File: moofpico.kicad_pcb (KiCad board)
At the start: 2 copper layers, 85.7 x 62.9 mm, 21 parts, among them J1 Conn_01x04, J100 Bus_Apple_II_Card_Side, J2 Micro_SD_Card_Det2, Q1 BS170, SW1 SW_DIP_x02, U2 74F11, U3 74LVC245, U4 74LVC245, U5 74LVC245, U6 RaspberryPi_Pico

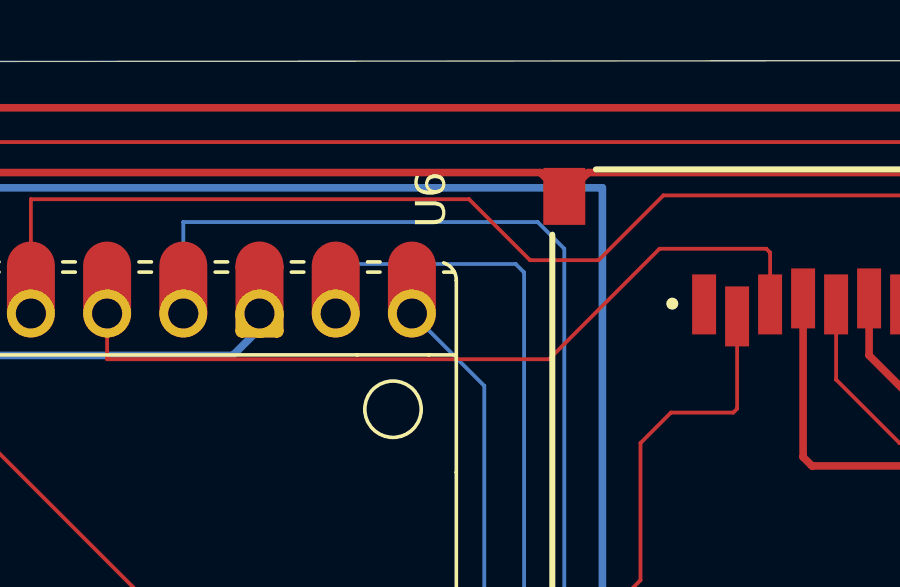
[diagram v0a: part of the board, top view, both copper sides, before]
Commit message: I do love how resynchronizing with the schematic changes all the UUIDs
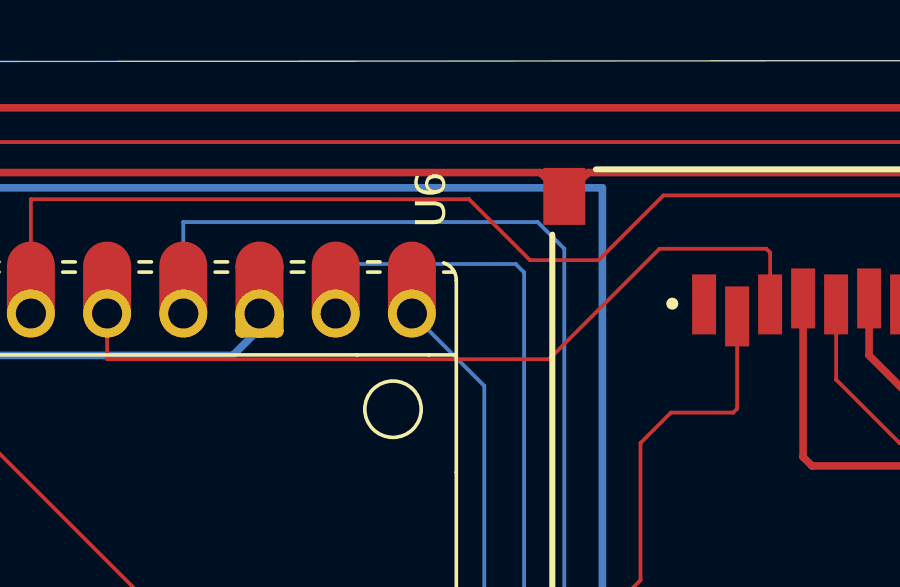
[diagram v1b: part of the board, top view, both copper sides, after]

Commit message: this side towards enemy
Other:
- board text added: "<- KBD"
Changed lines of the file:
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@@
 		(fp_arc
 			(start 10.579676 25.189937)
-			(mid 10.357946 25.493957)
+			(mid 10.357958 25.493991)
 			(end 10 25.61)
 			(stroke
@@
 		(layer "Edge.Cuts")
 	)
+	(gr_text "<- KBD"
+		(at 103.632 87.757 0)
+		(layer "F.SilkS")
+		(effects
+			(font
+				(size 0.8128 0.8128)
+				(thickness 0.1524)
+				(bold yes)
+			)
+			(justify left bottom)
+		)
+	)
 	(segment

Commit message: more faffing about with moving components
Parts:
- moved C5 1.15 mm to (172.0, 124.0)
- moved R4 0.66 mm to (174.5, 117.5)
- moved C3 0.31 mm to (171.0, 112.3)
- moved C1 0.26 mm to (174.0, 100.0)
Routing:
- net GND: track 366.8 -> 375.3 mm
- net +5V: track 48.2 -> 48.8 mm

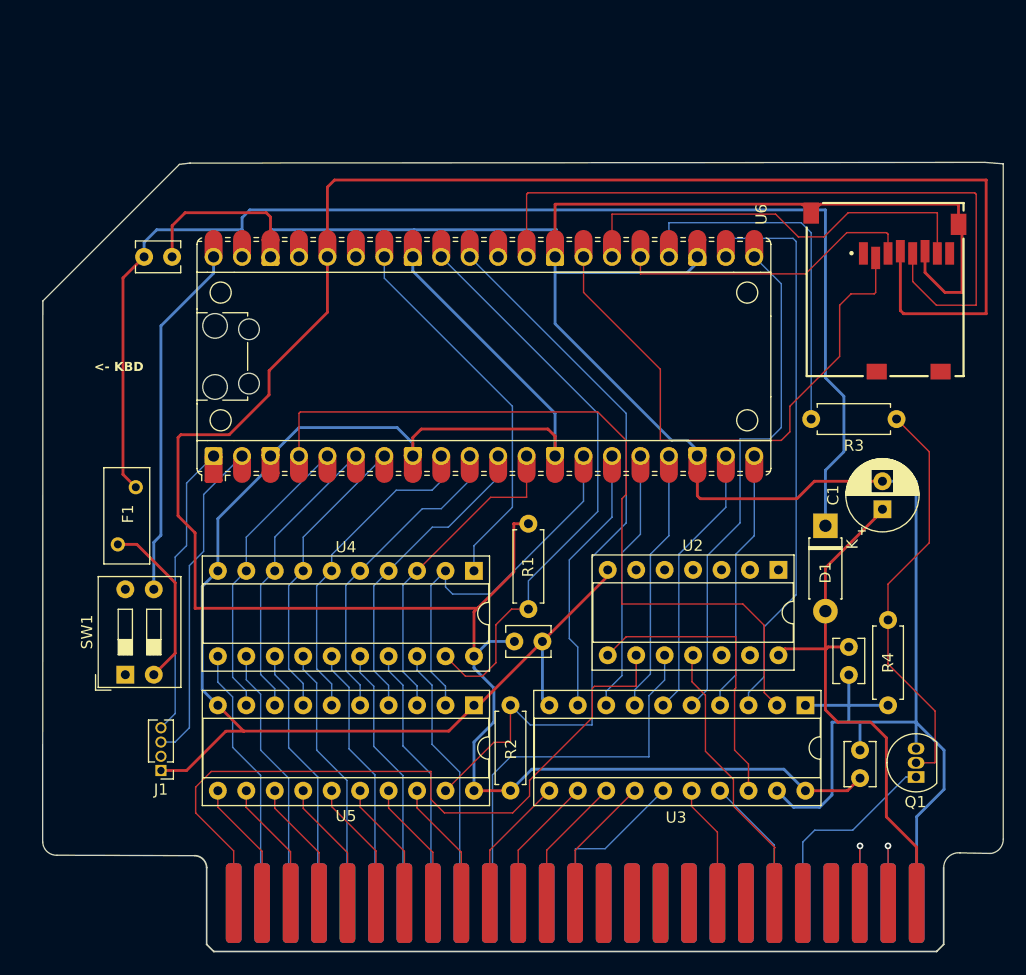
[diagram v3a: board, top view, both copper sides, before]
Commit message: checkpoint: kicad 8.0.1, move components around
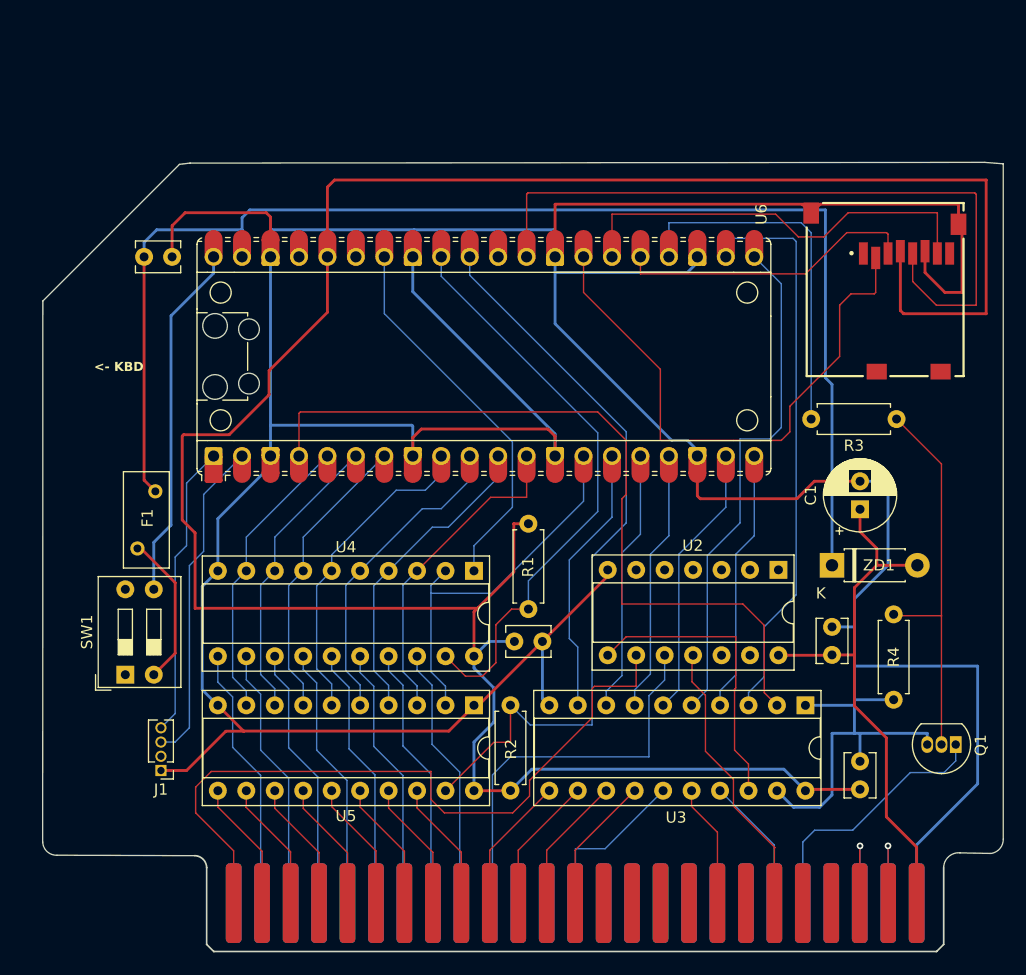
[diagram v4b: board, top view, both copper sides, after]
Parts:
- moved Q1 4.58 mm to (180.5, 121.0), turned to 180 degrees
- moved ZD1 3.58 mm to (169.5, 105.0), turned to 0 degrees
- moved C1 2.00 mm to (172.0, 100.0)
- moved F1 1.78 mm to (107.5, 103.5)
- moved C3 1.66 mm to (169.5, 113.0), turned to 90 degrees
- moved C5 1.00 mm to (172.0, 125.0)
- moved R4 0.71 mm to (175.0, 117.0)
- renumbered D1 to ZD1
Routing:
- net GND: track 375.3 -> 405.2 mm
- net Net-(J100-~{IRQ}): track 18.0 -> 23.6 mm
- net Net-(U6-VSYS): track 117.7 -> 119.7 mm
- net Net-(F1-Pad1): track 15.5 -> 13.6 mm
- net Net-(Q1-G): track 36.8 -> 35.0 mm
- net +3V3: track 224.3 -> 223.3 mm
- net +5V: track 48.8 -> 49.3 mm

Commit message: move footprint so that the card edges are aligned with the (mil) grid
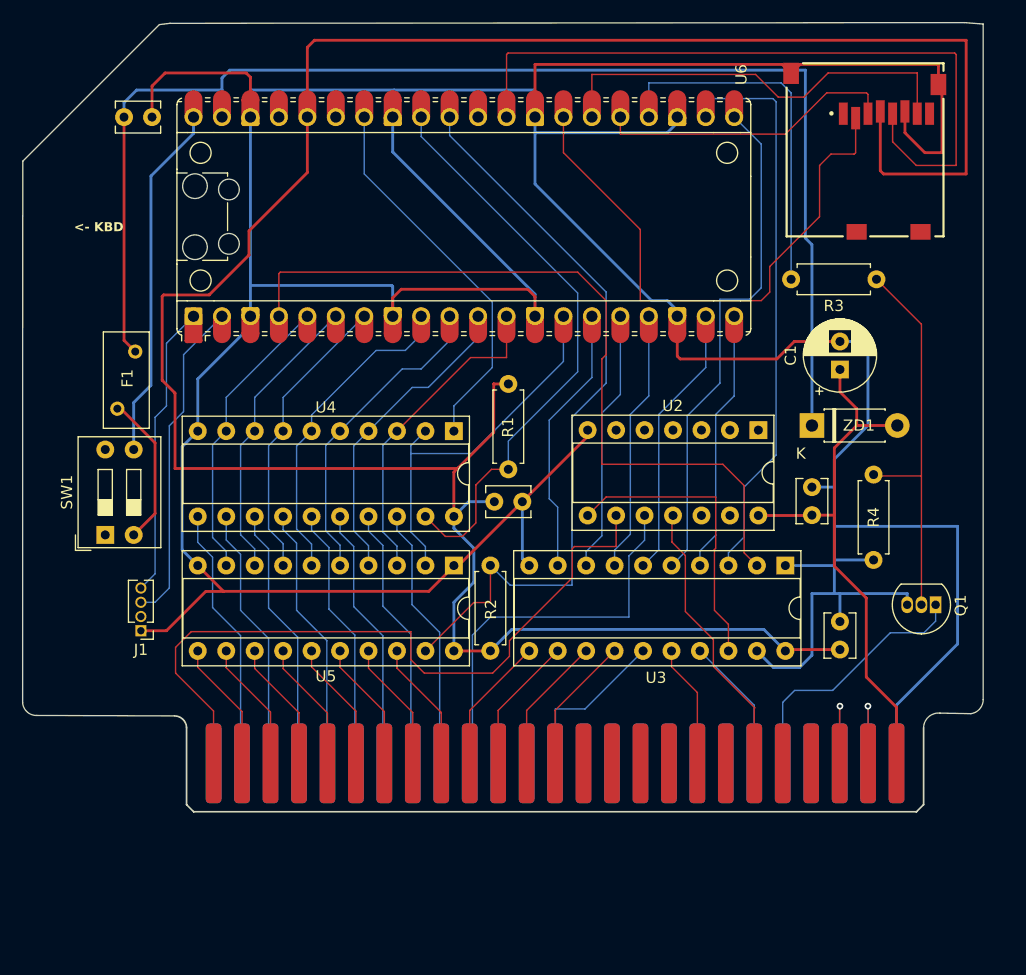
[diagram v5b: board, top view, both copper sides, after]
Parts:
- moved J100 12.6 mm to (144.8, 122.7)
- moved J2 12.6 mm to (172.4, 67.9)
- moved SW1 12.6 mm to (104.6, 102.3)
- moved C1 12.6 mm to (170.2, 87.5)
- moved C3 12.6 mm to (167.7, 100.5)
- moved C4 12.6 mm to (139.4, 99.3)
- moved C5 12.6 mm to (170.2, 112.5)
- moved F1 12.6 mm to (105.7, 91.0)
- moved J1 12.6 mm to (107.8, 110.8)
- moved Q1 12.6 mm to (178.7, 108.5)
- moved R1 12.6 mm to (140.6, 96.4)
- moved R2 12.6 mm to (139.0, 112.6)
- moved R3 12.6 mm to (173.5, 79.5)
- moved R4 12.6 mm to (173.2, 104.5)
- moved U2 12.6 mm to (162.9, 92.9)
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
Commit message: probably voodoo at this point, but: add another decoupling cap (although I seriously doubt it's needed at this point) provide enough space on the board so q1, c1, and f1 can all be bent flat
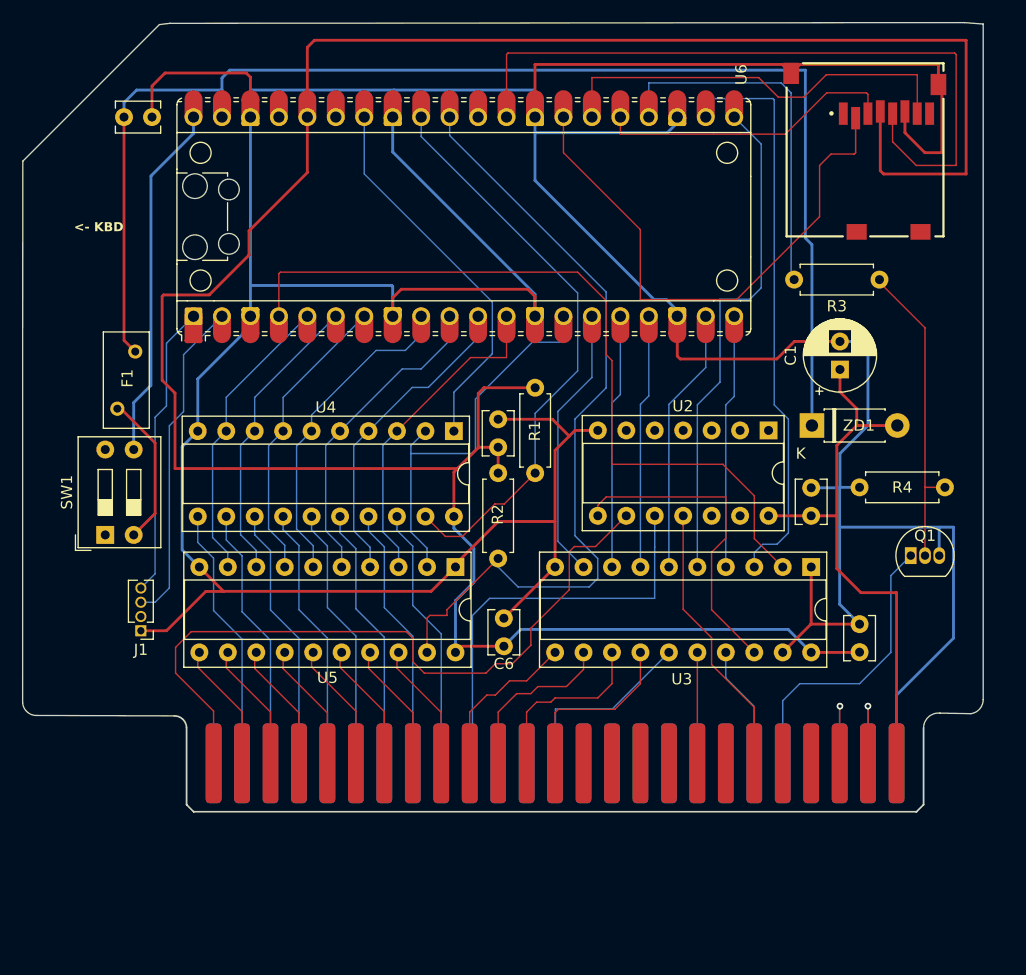
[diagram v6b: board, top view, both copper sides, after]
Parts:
- added C6: .1u, Capacitor_THT:C_Disc_D3.8mm_W2.6mm_P2.50mm, F.Cu at (140.2, 112.2)
- moved R2 15.9 mm to (139.7, 96.8), turned to -90 degrees
- moved R4 6.60 mm to (172.0, 98.0), turned to 0 degrees
- moved Q1 4.91 mm to (176.5, 104.1), turned to 0 degrees
- moved C4 4.87 mm to (139.7, 94.5), turned to 90 degrees
- moved R1 2.42 mm to (143.0, 96.8)
- moved U3 2.31 mm to (167.6, 105.2)
- moved C5 1.77 mm to (172.0, 112.8)
- moved U2 0.91 mm to (163.8, 93.0)
- moved R3 0.27 mm to (173.7, 79.5)
- moved U5 0.19 mm to (135.9, 105.2)
- moved C3 0.09 mm to (167.6, 100.6)
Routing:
- net Net-(Q1-G): track 35.0 -> 27.5 mm
- net GND: track 405.2 -> 410.3 mm
- net +3V3: track 223.3 -> 227.4 mm
- net AL/OE: track 67.7 -> 71.6 mm
- net TTLA10: track 12.2 -> 16.0 mm
- net TTLA11: track 12.2 -> 16.0 mm
- net TTLA9: track 12.2 -> 15.3 mm
- net Net-(J100-~{IRQ}): track 23.6 -> 26.4 mm
- net TTLPHI1: track 13.0 -> 15.3 mm
- net TTLENBL: track 26.4 -> 28.6 mm
- net TTLA8: track 12.2 -> 14.4 mm
- net Net-(J100-~{DEVICE_SELECT}): track 35.5 -> 37.2 mm
- net AD7: track 34.1 -> 35.7 mm
- net Net-(J2-DAT3/CD): track 51.0 -> 49.5 mm
- net TTL/RES: track 12.0 -> 11.0 mm
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
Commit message: more movin'
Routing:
- net AL/OE: track 71.6 -> 70.7 mm
- net TTLA10: track 16.0 -> 15.2 mm
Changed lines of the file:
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@@
 		)
 		(property "Value" "10K"
-			(at 3.81 2.37 -90)
+			(at -1.016 0 0)
 			(layer "F.Fab")
 			(effects
@@
 		)
 		(property "Value" ".1u"
-			(at 1.25 2.55 270)
+			(at -1.564 0 0)
 			(layer "F.Fab")
 			(effects
@@
 		)
 		(fp_text user "${REFERENCE}"
-			(at 1.25 0 270)
+			(at 1.25 0 90)
 			(layer "F.Fab")
 			(effects
@@
 		)
 		(property "Value" "10K"
-			(at 3.81 2.37 90)
+			(at 8.636 0 180)
 			(layer "F.Fab")
 			(effects
@@
 		)
 		(property "Value" ".1u"
-			(at 1.25 2.55 270)
+			(at 4.044 0 0)
 			(layer "F.Fab")
 			(effects
@@
 		)
 		(property "Value" "60R050XUL"
-			(at 2.6 5.4 -90)
+			(at 2.633 -2.33 -90)
 			(layer "F.Fab")
 			(effects
@@
 		)
 		(fp_text user "${REFERENCE}"
-			(at 3.81 0 -90)
+			(at 2.633 0.972 -90)
 			(layer "F.Fab")
 			(effects
@@
 		)
 		(property "Value" "SW_DIP_x02"
-			(at 3.81 5.96 -90)
+			(at 3.9925 -3.537 -90)
 			(layer "F.Fab")
 			(effects
@@
 		)
 		(property "Value" "RaspberryPi_Pico"
-			(at 0 27.94 90)
+			(at -1.807 0.268 0)
 			(unlocked yes)
 			(layer "F.Fab")
@@
 	)
 	(segment
-		(start 144.399 117.221)
-		(end 144.78 116.84)
+		(start 142.24 118.11)
+		(end 143.129 117.221)
 		(width 0.127)
 		(layer "F.Cu")
@@
 	)
 	(segment
-		(start 148.59 116.84)
-		(end 149.86 115.57)
+		(start 147.701 116.332)
+		(end 149.86 114.173)
 		(width 0.127)
 		(layer "F.Cu")
@@
 	)
 	(segment
-		(start 143.129 117.221)
-		(end 144.399 117.221)
+		(start 144.145 117.221)
+		(end 145.034 116.332)
 		(width 0.127)
 		(layer "F.Cu")
@@
 	)
 	(segment
-		(start 149.86 115.57)
-		(end 149.86 112.776)
+		(start 142.24 122.682)
+		(end 142.24 118.11)
 		(width 0.127)
 		(layer "F.Cu")
@@
 	)
 	(segment
-		(start 142.24 122.682)
-		(end 142.24 118.11)
+		(start 143.129 117.221)
+		(end 144.145 117.221)
 		(width 0.127)
 		(layer "F.Cu")
@@
 	)
 	(segment
-		(start 144.78 116.84)
-		(end 148.59 116.84)
+		(start 149.86 114.173)
+		(end 149.86 112.776)
 		(width 0.127)
 		(layer "F.Cu")
@@
 	)
 	(segment
-		(start 142.24 118.11)
-		(end 143.129 117.221)
+		(start 145.034 116.332)
+		(end 147.701 116.332)
 		(width 0.127)
 		(layer "F.Cu")
@@
 	)
 	(segment
-		(start 142.24 115.316)
-		(end 144.78 112.776)
+		(start 137.16 122.682)
+		(end 137.16 118.11)
 		(width 0.127)
 		(layer "F.Cu")
@@
 	)
 	(segment
-		(start 137.16 122.682)
-		(end 137.16 118.11)
+		(start 142.748 114.046)
+		(end 143.51 114.046)
 		(width 0.127)
 		(layer "F.Cu")
@@
 	(segment
 		(start 137.16 118.11)
-		(end 138.684 116.586)
+		(end 140.208 115.062)
 		(width 0.127)
 		(layer "F.Cu")
@@
 	)
 	(segment
-		(start 138.684 116.586)
-		(end 139.446 116.586)
+		(start 140.208 115.062)
+		(end 141.732 115.062)
 		(width 0.127)
 		(layer "F.Cu")
@@
 	)
 	(segment
-		(start 139.446 116.586)
-		(end 140.716 115.316)
+		(start 143.51 114.046)
+		(end 144.78 112.776)
 		(width 0.127)
 		(layer "F.Cu")
@@
 	)
 	(segment
-		(start 140.716 115.316)
-		(end 142.24 115.316)
+		(start 141.732 115.062)
+		(end 142.748 114.046)
 		(width 0.127)
 		(layer "F.Cu")
@@
 	)
 	(segment
-		(start 142.621 116.459)
-		(end 143.256 115.824)
+		(start 142.113 116.459)
+		(end 143.256 115.316)
 		(width 0.127)
 		(layer "F.Cu")
@@
 	)
 	(segment
-		(start 143.256 115.824)
-		(end 145.796 115.824)
+		(start 143.256 115.316)
+		(end 144.526 115.316)
 		(width 0.127)
 		(layer "F.Cu")
@@
 	(segment
 		(start 141.351 116.459)
-		(end 142.621 116.459)
+		(end 142.113 116.459)
 		(width 0.127)
 		(layer "F.Cu")
@@
 	)
 	(segment
-		(start 145.796 115.824)
-		(end 147.32 114.3)
+		(start 139.7 122.682)
+		(end 139.7 118.11)
 		(width 0.127)
 		(layer "F.Cu")
@@
 	)
 	(segment
-		(start 139.7 122.682)
-		(end 139.7 118.11)
+		(start 147.32 113.538)
+		(end 147.32 112.776)
 		(width 0.127)
 		(layer "F.Cu")
@@
 	)
 	(segment
-		(start 147.32 114.3)
-		(end 147.32 112.776)
+		(start 146.304 114.554)
+		(end 147.32 113.538)
+		(width 0.127)
+		(layer "F.Cu")
+		(net 12)
+	)
+	(segment
+		(start 144.526 115.316)
+		(end 145.288 114.554)
+		(width 0.127)
+		(layer "F.Cu")
+		(net 12)
+	)
+	(segment
+		(start 145.288 114.554)
+		(end 146.304 114.554)
 		(width 0.127)
 		(layer "F.Cu")
@@
 	)
 	(segment
-		(start 133.35 109.728)
+		(start 133.35 110.744)
 		(end 133.35 112.776)
 		(width 0.127)
@@
 	(segment
 		(start 139.7 104.394)
-		(end 135.128 108.966)
-		(width 0.127)
-		(layer "F.Cu")
-		(net 21)
-	)
-	(segment
-		(start 133.604 109.474)
-		(end 133.35 109.728)
-		(width 0.127)
-		(layer "F.Cu")
-		(net 21)
-	)
-	(segment
-		(start 135.128 108.966)
-		(end 135.128 109.474)
-		(width 0.127)
-		(layer "F.Cu")
-		(net 21)
-	)
-	(segment
-		(start 135.128 109.474)
-		(end 133.604 109.474)
+		(end 133.35 110.744)
 		(width 0.127)
 		(layer "F.Cu")
